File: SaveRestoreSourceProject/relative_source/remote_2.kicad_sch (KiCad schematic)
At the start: 3 parts

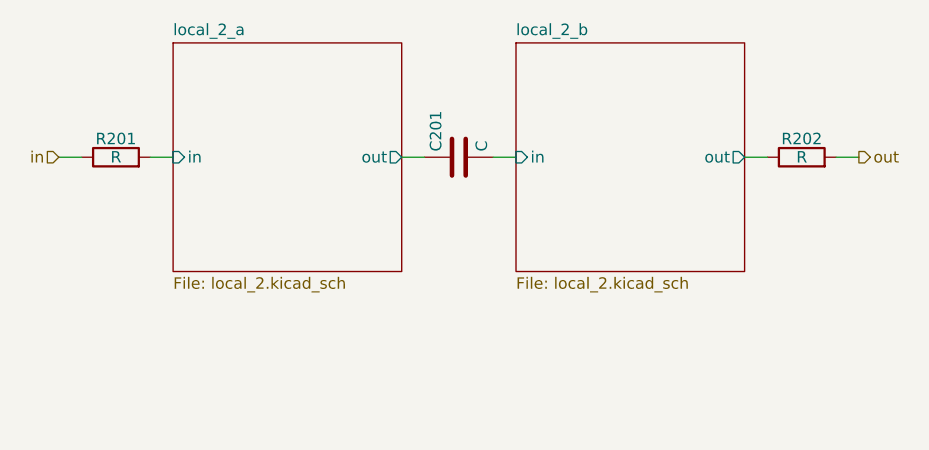
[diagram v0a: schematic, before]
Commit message: Add support for connected drawings, update test template
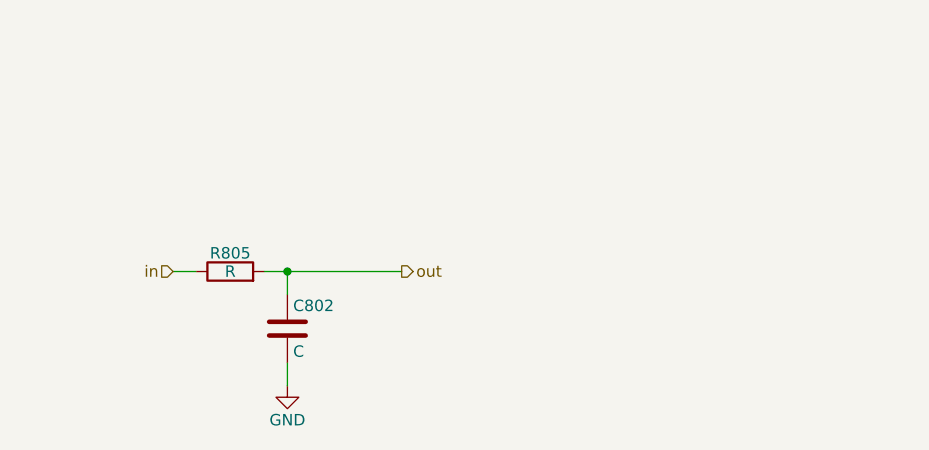
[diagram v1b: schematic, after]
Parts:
- removed C201: C, Capacitor_SMD:C_1206_3216Metric, symbol Device:C
- removed R201, R202: R, Resistor_SMD:R_1206_3216Metric, symbol Device:R
- added C802: C, Capacitor_SMD:C_1206_3216Metric, symbol Device:C
- added R805: R, Resistor_SMD:R_1206_3216Metric, symbol Device:R
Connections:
- net in: now also R805.1
- net out: now also C802.1, R805.2
- new net GND: C802.2
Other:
- removed sheet local_2_a
- removed sheet local_2_b
